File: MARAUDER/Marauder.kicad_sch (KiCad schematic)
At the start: 23 parts, among them J1 Conn_01x08_Socket, J2 Conn_01x08_Socket, J3 Conn_01x10_Socket, J4 GPS, J5 Conn_01x10_Socket, P1 USB_C_Plug_USB2.0, Q1 DMP2004TK-7, Q2 DMP2004TK-7, SW1 RESET, SW2 GPIO, U2 ESP32-S3-WROOM-1U-N4

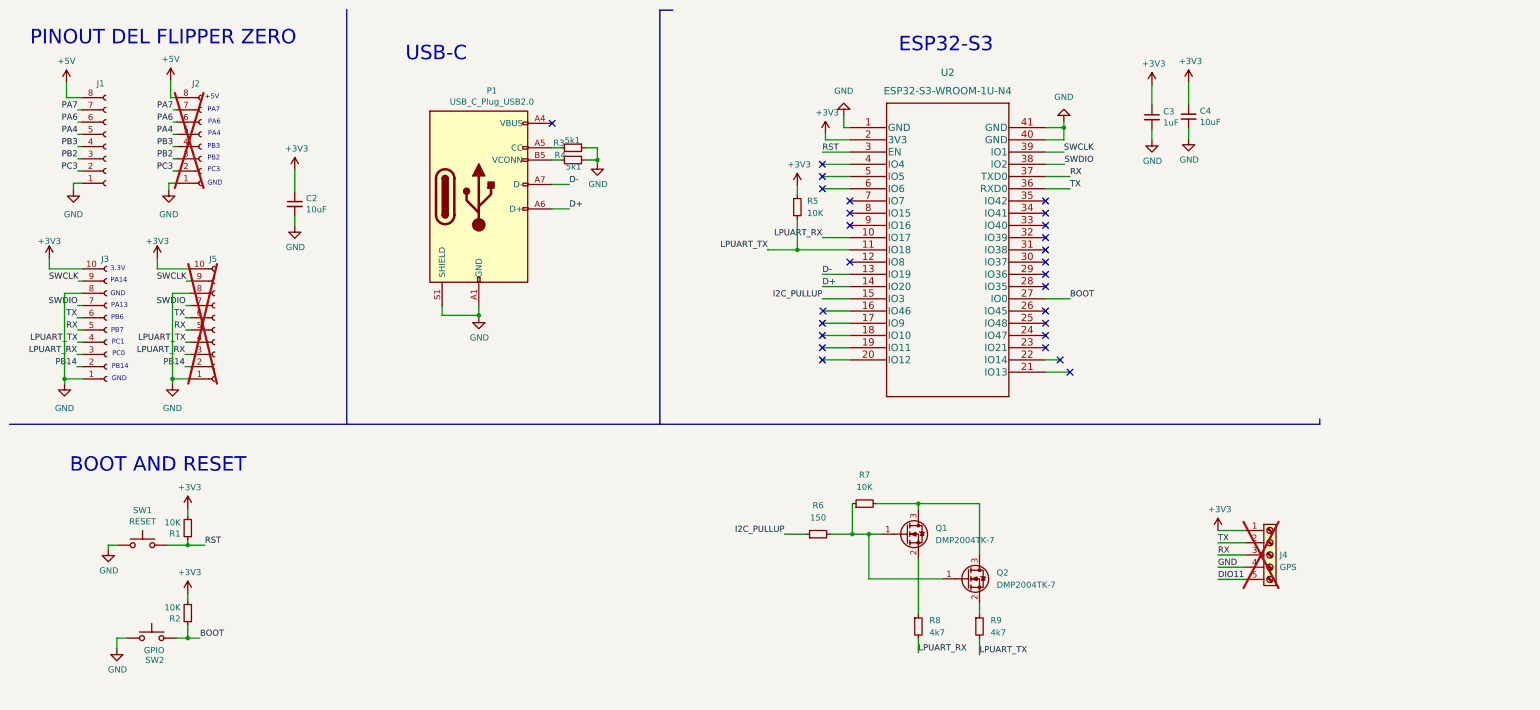
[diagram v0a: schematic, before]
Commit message: feat(Hw):ESP32-C5-Added
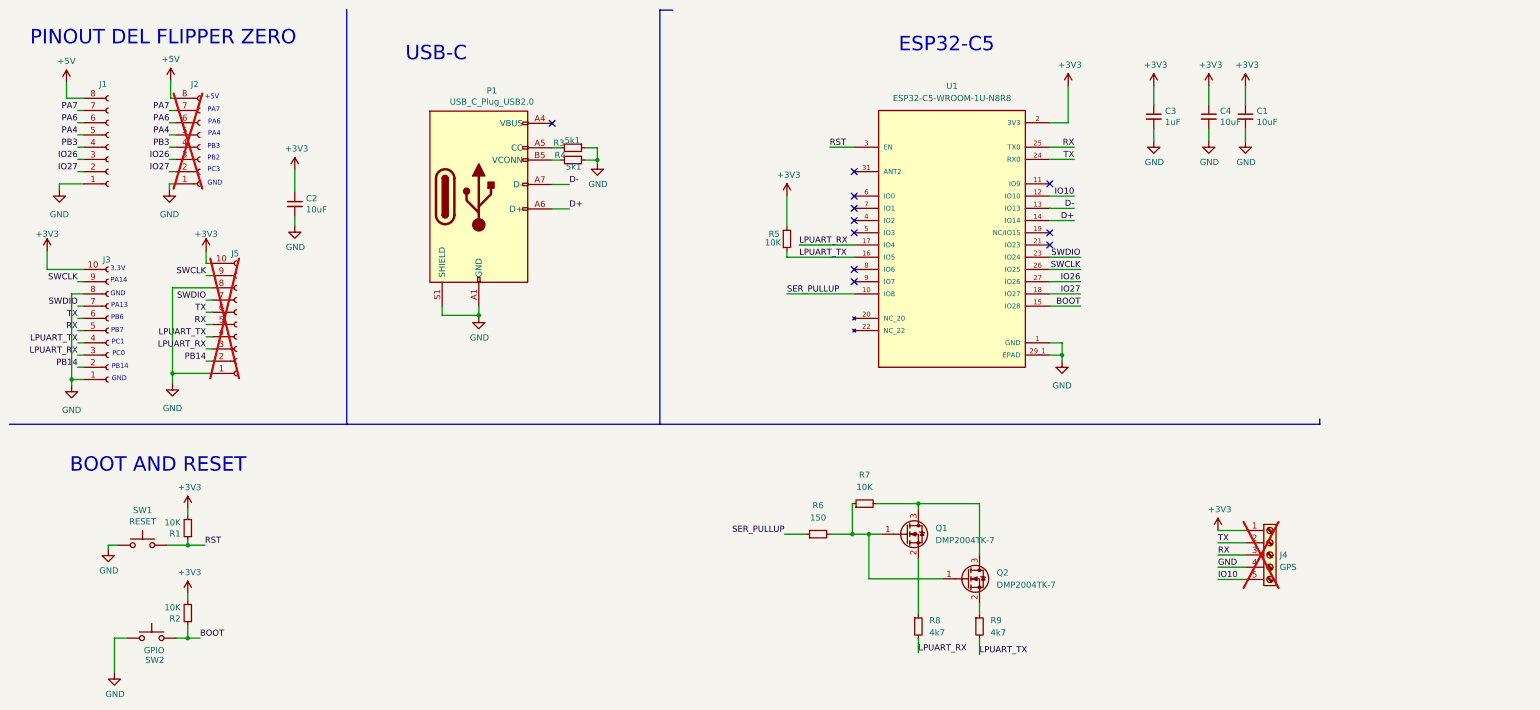
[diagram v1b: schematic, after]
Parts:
- removed U2: ESP32-S3-WROOM-1U-N4, RF_Module:ESP32-S3-WROOM-1U, symbol ESP32-S3-WROOM:ESP32-S3-WROOM-1-N8
- added C1: 10uF, Capacitor_SMD:C_0603_1608Metric, symbol Device:C_Small
- added U1: ESP32-C5-WROOM-1U-N8R8, Marauder:XCVR_ESP32-C5-WROOM-1U-N8R8, symbol ESP32-C5-WROOM-1U-N8R8:ESP32-C5-WROOM-1U-N8R8
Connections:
- net +3V3: now also C1.1, U1.2 (3V3)
- net BOOT: now also U1.15 (IO28)
- net D+: now also U1.14 (IO14)
- net D-: now also U1.13 (IO13)
- net LPUART_RX: now also U1.17 (IO4)
- net LPUART_TX: now also U1.16 (IO5)
- net RST: now also U1.3 (EN)
- net RX: now also U1.25 (TX0)
- net SWCLK: now also U1.26 (IO25)
- net SWDIO: now also U1.23 (IO24)
- net TX: now also U1.24 (RX0)
- net DIO11 renamed IO10
- net IO10: now also U1.12 (IO10)
- net GND renamed EPAD
- net EPAD: now also C1.2, U1.1 (GND), U1.28 (GND), U1.29_1 (EPAD), U1.29_2 (EPAD), U1.29_3 (EPAD), U1.29_4 (EPAD), U1.29_5 (EPAD), U1.29_6 (EPAD), U1.29_7 (EPAD), U1.29_8 (EPAD), U1.29_9 (EPAD), U1.30 (GND), U1.32 (GND)
- net I2C_PULLUP renamed SER_PULLUP
- net SER_PULLUP: now also U1.10 (IO8)
- net PB2 renamed IO26
- net IO26: now also U1.27 (IO26)
- net PC3 renamed IO27
- net IO27: now also U1.18 (IO27)
- no-connect marks 27 -> 11
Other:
- note added: "ESP32-C5"
- note removed: "ESP32-S3"
- moved on the sheet: C4, J1, J5, R5

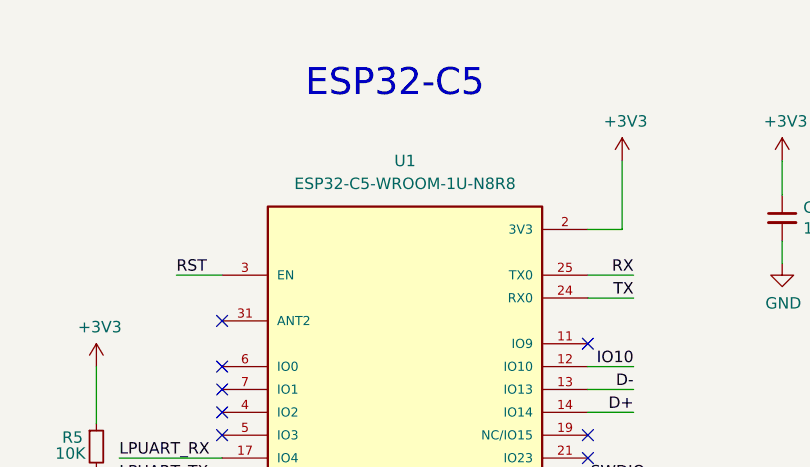
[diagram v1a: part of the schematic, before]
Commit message: feat(Hw):Update_BoM
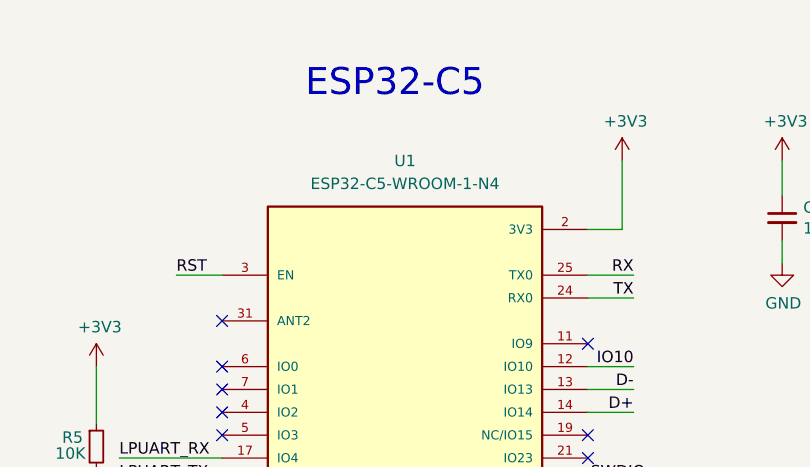
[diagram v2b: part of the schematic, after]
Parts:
- U1: value ESP32-C5-WROOM-1U-N8R8 -> ESP32-C5-WROOM-1-N4; manf# (none) -> 356-ESP32C5WROM1N4
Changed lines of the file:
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@@
 			)
 		)
-		(property "Value" "ESP32-C5-WROOM-1U-N8R8"
+		(property "Value" "ESP32-C5-WROOM-1-N4"
 			(at 208.28 30.48 0)
 			(effects
@@
 				(hide yes)
 			)
+		)
+		(property "manf#" "356-ESP32C5WROM1N4"
+			(at 208.28 58.42 0)
+			(effects
+				(font
+					(size 1.27 1.27)
+				)
+				(hide yes)
+			)

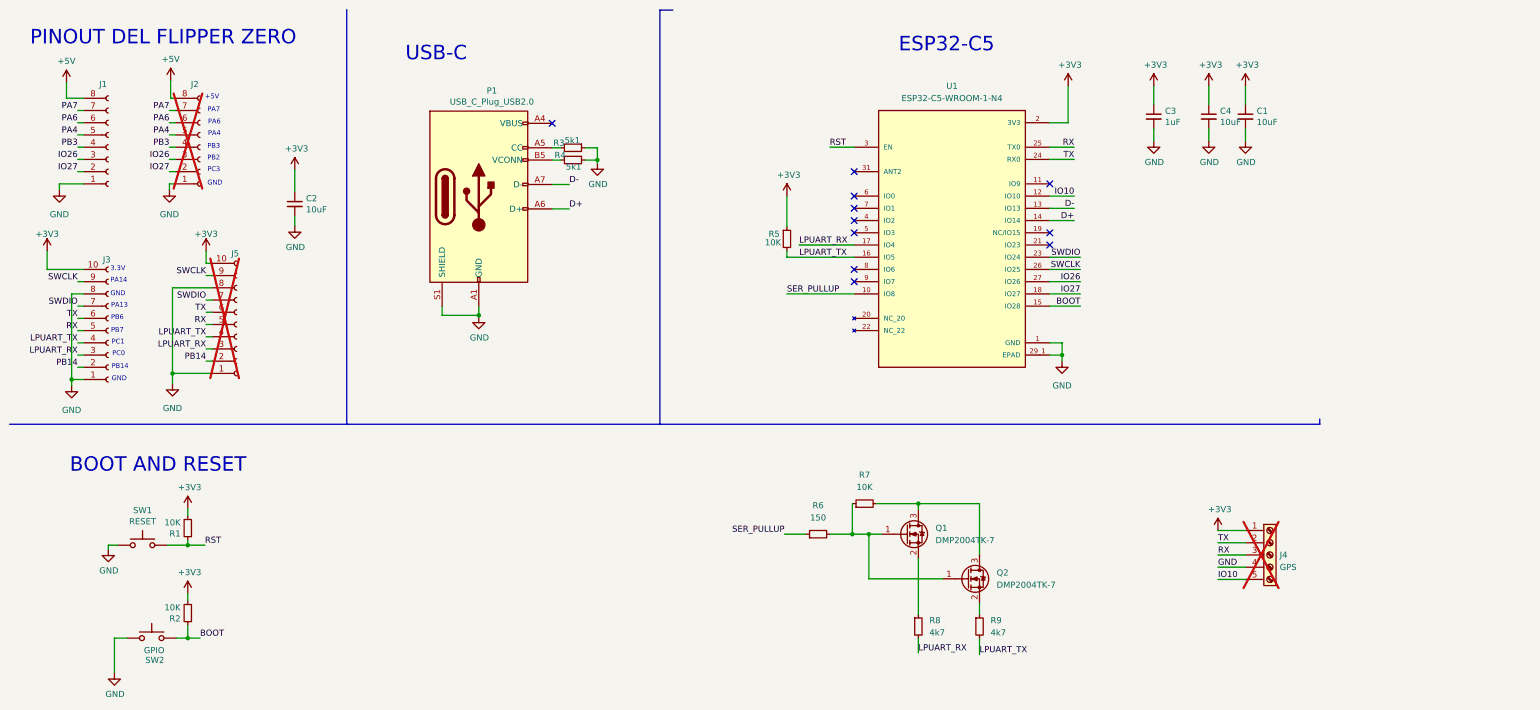
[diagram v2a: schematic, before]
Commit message: feat(Hw): 3d_Added_Update_Route
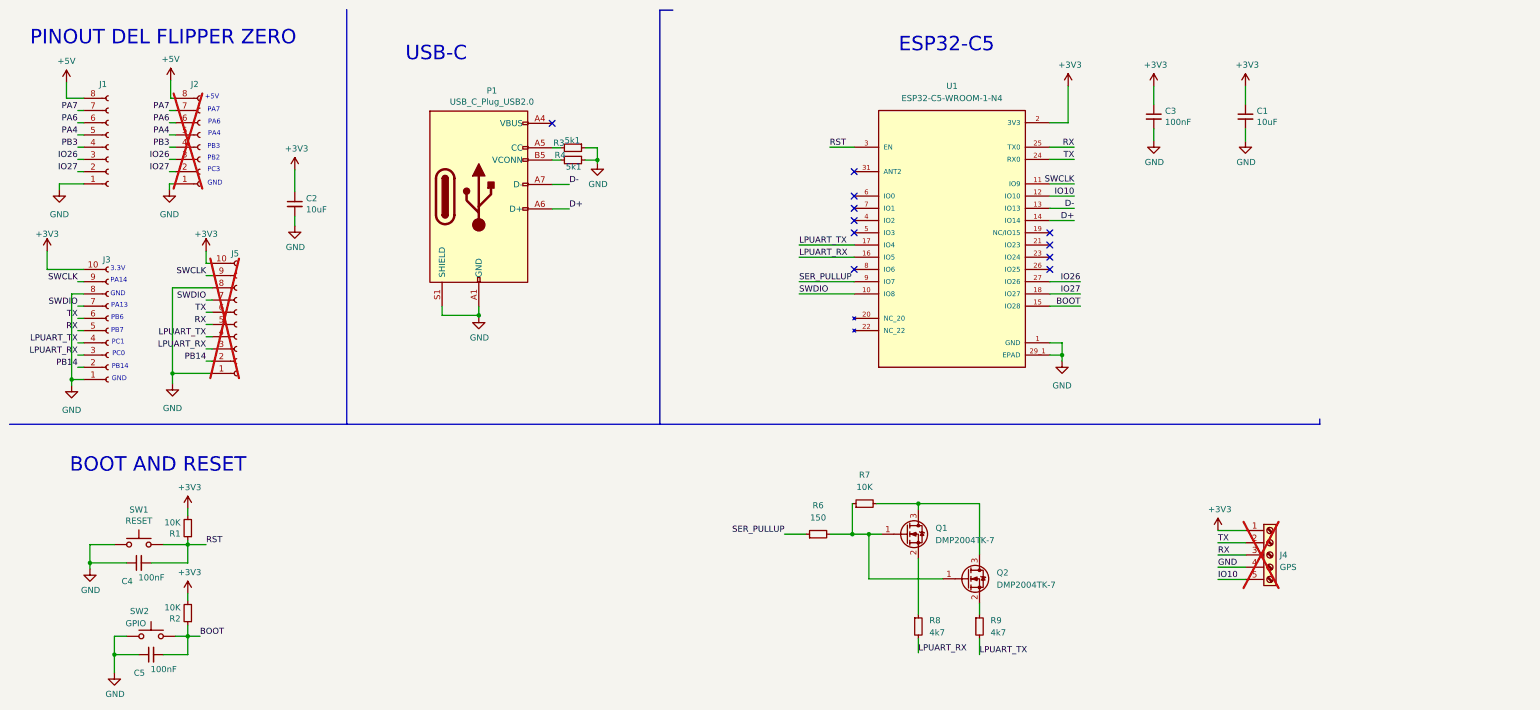
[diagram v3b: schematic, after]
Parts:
- removed R5: 10K, Resistor_SMD:R_0603_1608Metric, symbol Device:R_Small
- added C5: 100nF, Capacitor_SMD:C_0603_1608Metric, symbol Device:C_Small
- C3: value 1uF -> 100nF; LCSC# C15849 -> C597251
- C4: value 10uF -> 100nF; LCSC# C85713 -> C597251
- SW1, SW2: LCSC# (none) -> C2886897
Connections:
- net +3V3: no longer C4.1
- net BOOT: now also C5.2
- net EPAD: now also C4.1, C5.1; no longer C4.2
- net LPUART_RX: now also U1.16 (IO5); no longer U1.17 (IO4)
- net LPUART_TX: now also U1.17 (IO4); no longer U1.16 (IO5)
- net RST: now also C4.2
- net SER_PULLUP: now also U1.9 (IO7); no longer U1.10 (IO8)
- net SWCLK: now also U1.11 (IO9); no longer U1.26 (IO25)
- net SWDIO: now also U1.10 (IO8); no longer U1.23 (IO24)
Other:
- moved on the sheet: SW1

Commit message: feat: add GPS schematic
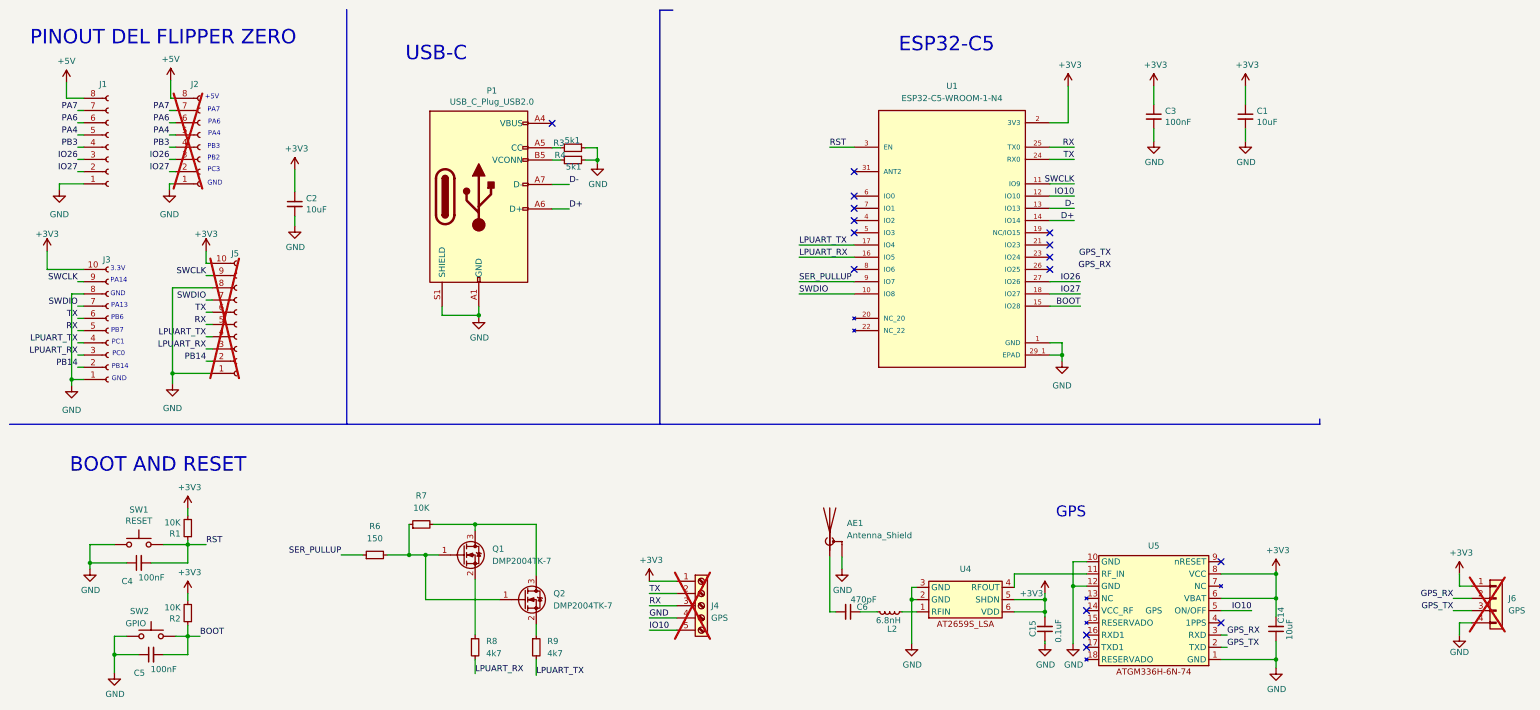
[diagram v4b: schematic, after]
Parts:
- added AE1: Antenna_Shield, Connector_Coaxial:U.FL_Molex_MCRF_73412-0110_Vertical, symbol Device:Antenna_Shield
- added C14: 10uF, Capacitor_SMD:C_0603_1608Metric, symbol Device:C_Small
- added C15: 0.1uF, Capacitor_SMD:C_0603_1608Metric, symbol Device:C_Small
- added C6: 470pF, Capacitor_SMD:C_0603_1608Metric, symbol Device:C_Small
- added J6: GPS, Connector_PinHeader_2.54mm:PinHeader_1x04_P2.54mm_Vertical, symbol Connector_Generic:Conn_01x04
- added L2: 6.8nH, Inductor_SMD:L_0603_1608Metric_Pad1.05x0.95mm_HandSolder, symbol Device:L_Small
- added U4: LNA, Footprints:AT2659S-LSA, symbol Minino:AT2659S_LSA
- added U5: GPS, Footprints:GPSM-SMD_ATGM336H, symbol Minino:ATGM336H-6N-74
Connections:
- net +3V3: now also C14.2, C15.2, J6.1 (Pin_1), U4.5 (SHDN), U4.6 (VDD), U5.6 (VBAT), U5.8 (VCC)
- net EPAD: now also AE1.2 (Shield), C14.1, C15.1, J6.4 (Pin_4), U4.2 (GND), U4.3 (GND), U5.1 (GND), U5.10 (GND), U5.12 (GND)
- net IO10: now also U5.5 (ON/OFF)
- new net: C6.1, L2.2
- new net: AE1.1 (A), C6.2
- new net: L2.1, U4.1 (RFIN)
- new net: U4.4 (RFOUT), U5.11 (RF_IN)
- new net GPS_RX: J6.2 (Pin_2), U5.3 (RXD)
- new net GPS_TX: J6.3 (Pin_3), U5.2 (TXD)
- no-connect marks 11 -> 16
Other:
- note added: "GPS"
- moved on the sheet: J4, Q1, Q2, R6, R7, R8, R9

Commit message: feat(Hw):Update_PCB
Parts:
- removed J6: GPS, Connector_PinHeader_2.54mm:PinHeader_1x04_P2.54mm_Vertical, symbol Connector_Generic:Conn_01x04
- P1: footprint Connectors:C393939 -> Marauder:C393939
- U4: footprint Footprints:AT2659S-LSA -> Marauder:AT2659S-LSA
- U5: footprint Footprints:GPSM-SMD_ATGM336H -> Marauder:GPSM-SMD_ATGM336H
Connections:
- net GPS_RX: now also U1.26 (IO25)
- net GPS_TX: now also U1.23 (IO24)
- no-connect marks 16 -> 14

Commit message: feat(Hw):version_updated
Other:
- company: (none) -> ElectronicCats
- title: (none) -> flipper-aad-on-Marauder
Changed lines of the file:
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@@
 	(generator_version "9.0")
 	(paper "A4")
+	(title_block
+		(title "flipper-aad-on-Marauder")
+		(date "2026-05-11")
+		(rev "v2.2")
+		(company "ElectronicCats")
+		(comment 1 "Edgar Capuchino")
+	)
 	(text "PB6"
 		(exclude_from_sim no)
